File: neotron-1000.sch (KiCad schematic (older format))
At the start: 0 parts

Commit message: Initial peripheral layout and Cadding
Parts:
- added J?: Micro_SD_Card_Det, symbol Connector:Micro_SD_Card_Det
- added U?: STM32H743ZITx, Package_QFP:LQFP-144_20x20mm_P0.5mm, symbol MCU_ST_STM32H7:STM32H743ZITx
- added U?: AS4C4M16SA, TSOPII-54, symbol Memory_RAM:AS4C4M16SA
- added U?: TUSB2036, Package_QFP:LQFP-32_7x7mm_P0.8mm, symbol Interface_USB:TUSB2036
- added U?: TPS2042D, Package_SO:SOIC-8_3.9x4.9mm_P1.27mm, symbol Power_Management:TPS2042D
- added U?: ENC28J60x-SO, Package_SO:SOIC-28W_7.5x17.9mm_P1.27mm, symbol Interface_Ethernet:ENC28J60x-SO
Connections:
- new net: U?.10 (~OVRCUR1), U?.8 (~OC1)
- new net: U?.13 (~PWRON2), U?.4 (~EN2)
- new net: U?.14 (~OVRCUR2), U?.5 (~OC2)
- new net: U?.3 (~EN1), U?.9 (~PWRON1)
- new net ETH_SPI_MISO: U?.28 (PC2_C), U?.6 (SO)
- new net ETH_SPI_MOSI: U?.27 (PC1), U?.7 (SI)
- new net ETH_SPI_SCK: U?.101 (PA9), U?.8 (SCK)
- new net FMC_A0: U?.10 (PF0)
- new net FMC_A1: U?.11 (PF1)
- new net FMC_A10: U?.56 (PG0)
- new net FMC_A2: U?.12 (PF2)
- new net FMC_A3: U?.13 (PF3)
- new net FMC_A4: U?.14 (PF4)
- new net FMC_A5: U?.15 (PF5)
- new net FMC_A6: U?.50 (PF12)
- new net FMC_A7: U?.53 (PF13)
- new net FMC_A8: U?.54 (PF14)
- new net FMC_A9: U?.55 (PF15)
- new net FMC_BA0: U?.89 (PG4)
- new net FMC_CKE0: U?.29 (PC3_C)
- new net FMC_CLK: U?.93 (PG8)
- new net FMC_D0: U?.85 (PD14)
- new net FMC_D1: U?.86 (PD15)
- new net FMC_D2: U?.114 (PD0)
- new net FMC_D3: U?.115 (PD1)
- new net FMC_D4: U?.58 (PE7)
- new net FMC_D5: U?.59 (PE8)
- new net FMC_D6: U?.60 (PE9)
- new net FMC_D7: U?.63 (PE10)
- new net GND: J?.6 (VSS), U?.1 (GND), U?.107 (VSS), U?.11 (VSSRX), U?.120 (VSS), U?.130 (VSS), U?.16 (VSS), U?.18 (VSSTX), U?.2 (VSS), U?.21 (VSSPLL), U?.21 (~OCPROT~/~PWRSW~), U?.22 (NPINT0), U?.22 (VSSOSC), U?.23 (NPINT1), U?.28 (GND), U?.31 (MODE), U?.31 (VSSA), U?.38 (VSS), U?.51 (VSS), U?.61 (VSS), U?.7 (GND), U?.83 (VSS), U?.9 (~CS), U?.94 (VSS)
- new net GPU_INT: U?.118 (PD4)
- new net GPU_SPI_CLK: U?.126 (PG11)
- new net GPU_SPI_MIS0: U?.124 (PG9)
- new net GPU_SPI_MOSI: U?.123 (PD7)
- new net HEADER_00: U?.34 (PA0)
- new net HEADER_01: U?.100 (PA8)
- new net HEADER_02: U?.135 (PB5)
- new net HEADER_03: U?.73 (PB12)
- new net HEADER_04: U?.74 (PB13)
- new net HEADER_05: U?.7 (PC13)
- new net HEADER_06: U?.8 (PC14)
- new net HEADER_07: U?.9 (PC15)
- new net HEADER_08: U?.80 (PD11)
- new net HEADER_09: U?.141 (PE0)
- new net HEADER_10: U?.142 (PE1)
- new net HEADER_11: U?.2 (PE3)
- new net HEADER_12: U?.57 (PG1)
- new net HEADER_13: U?.87 (PG2)
- new net HEADER_14: U?.88 (PG3)
- new net HEADER_15: U?.90 (PG5)
- new net HEADER_16: U?.91 (PG6)
- new net HEADER_17: U?.127 (PG12)
- new net HEADER_18: U?.129 (PG14)
- new net HEADER_SPI_MISO: U?.66 (PE13)
- new net HEADER_SPI_MOSI: U?.67 (PE14)
- new net HEADER_SPI_SCK: U?.1 (PE2)
- new net HEADER_UART_RX: U?.78 (PD9)
- new net HEADER_UART_TX: U?.77 (PD8)
- new net I2C_HEADER_SCL: U?.81 (PD12)
- new net I2C_HEADER_SDA: U?.82 (PD13)
- new net I2C_INT_SCL: U?.136 (PB6)
- new net I2C_INT_SDA: U?.137 (PB7)
- new net I2S_SCK: U?.133 (PB3)
- new net I2S_SDI: U?.134 (PB4)
- new net I2S_SDO: U?.48 (PB2)
- new net I2S_WS: U?.110 (PA15)
- new net LTDC_B0: U?.3 (PE4)
- new net LTDC_B1: U?.102 (PA10)
- new net LTDC_B2: U?.125 (PG10)
- new net LTDC_B3: U?.79 (PD10)
- new net LTDC_B4: U?.65 (PE12)
- new net LTDC_B5: U?.37 (PA3)
- new net LTDC_B6: U?.139 (PB8)
- new net LTDC_B7: U?.140 (PB9)
- new net LTDC_CLK: U?.92 (PG7)
- new net LTDC_DE: U?.22 (PF10)
- new net LTDC_G0: U?.4 (PE5)
- new net LTDC_G1: U?.5 (PE6)
- new net LTDC_G2: U?.42 (PA6)
- new net LTDC_G3: U?.64 (PE11)
- new net LTDC_G4: U?.69 (PB10)
- new net LTDC_G5: U?.70 (PB11)
- new net LTDC_G6: U?.97 (PC7)
- new net LTDC_G7: U?.117 (PD3)
- new net LTDC_HSYNC: U?.96 (PC6)
- new net LTDC_R0: U?.128 (PG13)
- new net LTDC_R1: U?.36 (PA2)
- new net LTDC_R2: U?.35 (PA1)
- new net LTDC_R3: U?.46 (PB0)
- new net LTDC_R4: U?.41 (PA5)
- new net LTDC_R5: U?.26 (PC0)
- new net LTDC_R6: U?.47 (PB1)
- new net LTDC_R7: U?.68 (PE15)
- new net LTDC_VSYNC: U?.40 (PA4)
- new net PS2_KBD_CLK: U?.19 (PF7)
- new net PS2_KBD_DAT: U?.18 (PF6)
- new net PS2_MSE_CLK: U?.21 (PF9)
- new net PS2_MSE_DAT: U?.20 (PF8)
- new net SDMMC_CK: J?.5 (CLK), U?.113 (PC12)
- new net SDMMC_CMD: J?.3 (CMD), U?.116 (PD2)
- new net SDMMC_D0: J?.7 (DAT0), U?.98 (PC8)
- new net SDMMC_D1: J?.8 (DAT1), U?.99 (PC9)
- new net SDMMC_D2: J?.1 (DAT2), U?.111 (PC10)
- new net SDMMC_D3: J?.2 (DAT3/CD), U?.112 (PC11)
- new net SWCLK: U?.109 (PA14)
- new net SWDIO: U?.105 (PA13)
- new net UART_RX: U?.122 (PD6)
- new net UART_TX: U?.119 (PD5)
- new net USB1_PWR: U?.7 (OUT1)
- new net USB2_PWR: U?.6 (OUT2)
- new net USB_C_DM: U?.103 (PA11)
- new net USB_C_DP: U?.104 (PA12)
- new net USB_HOST_DM: U?.75 (PB14)
- new net USB_HOST_DP: U?.76 (PB15)
- new net VBUS: U?.2 (IN1)
- new net VCC: J?.4 (VDD), U?.108 (VDD), U?.121 (VDD), U?.131 (VDD), U?.144 (VDD), U?.15 (VDDTX), U?.17 (VDD), U?.19 (VDDRX), U?.20 (VDDPLL), U?.24 (~NP3), U?.25 (VCC), U?.25 (VDDOSC), U?.26 (~EXTMEM), U?.28 (VDD), U?.3 (VCC), U?.30 (VDD), U?.33 (VDDA), U?.39 (VDD), U?.52 (VDD), U?.6 (EEDATA/~GANGED), U?.6 (VBAT), U?.62 (VDD), U?.72 (VDD), U?.8 (~BUSPWR), U?.84 (VDD), U?.95 (VDD33_USB)
- new net ~ETH_INT: U?.4 (~INT), U?.45 (PC5)
- new net ~FMC_CAS: U?.132 (PG15)
- new net ~FMC_E0: U?.44 (PC4)
- new net ~FMC_RAS: U?.49 (PF11)
- new net ~FMC_WE: U?.43 (PA7)
- new net ~RESET: U?.10 (~RESET), U?.25 (NRST), U?.4 (~RESET)
- no-connect marks 0 -> 10

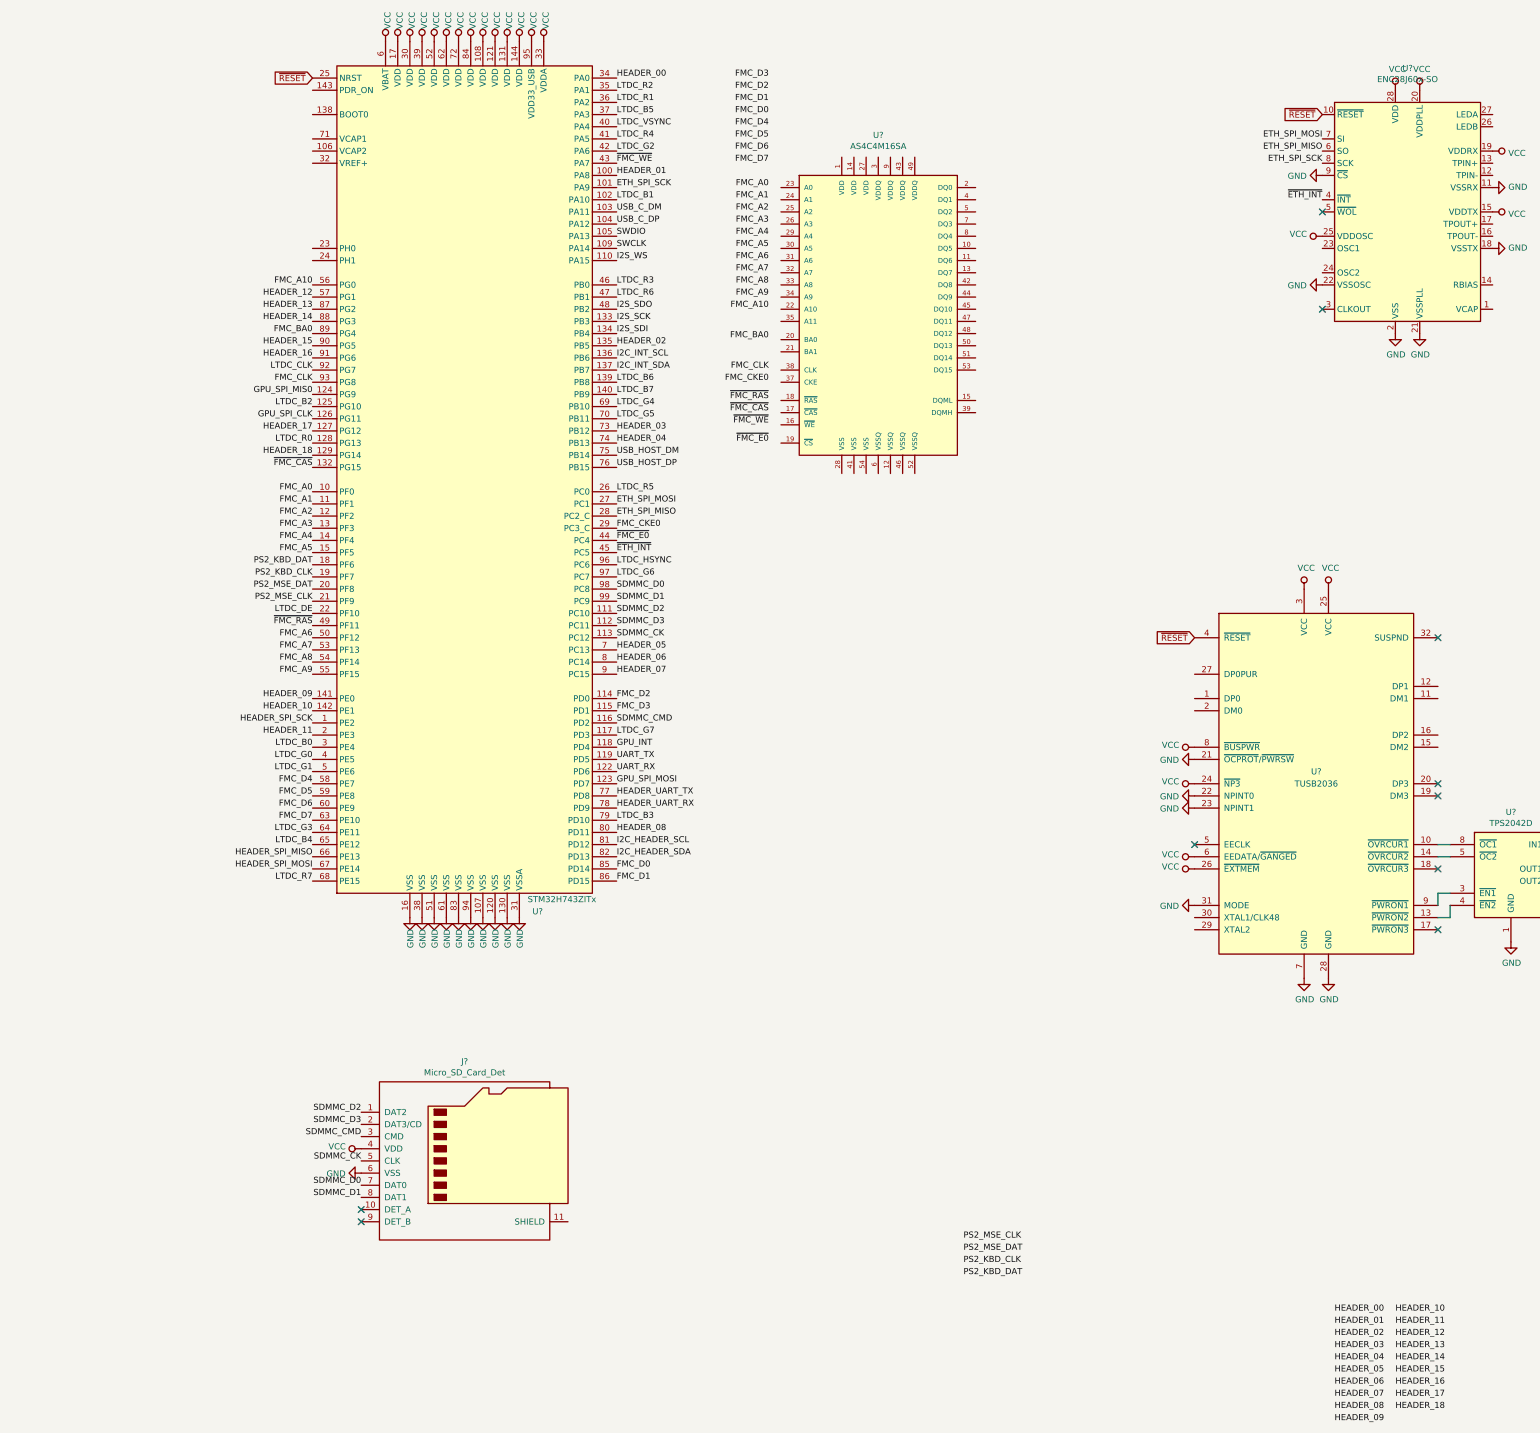
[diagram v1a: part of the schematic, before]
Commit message: added Pi Port
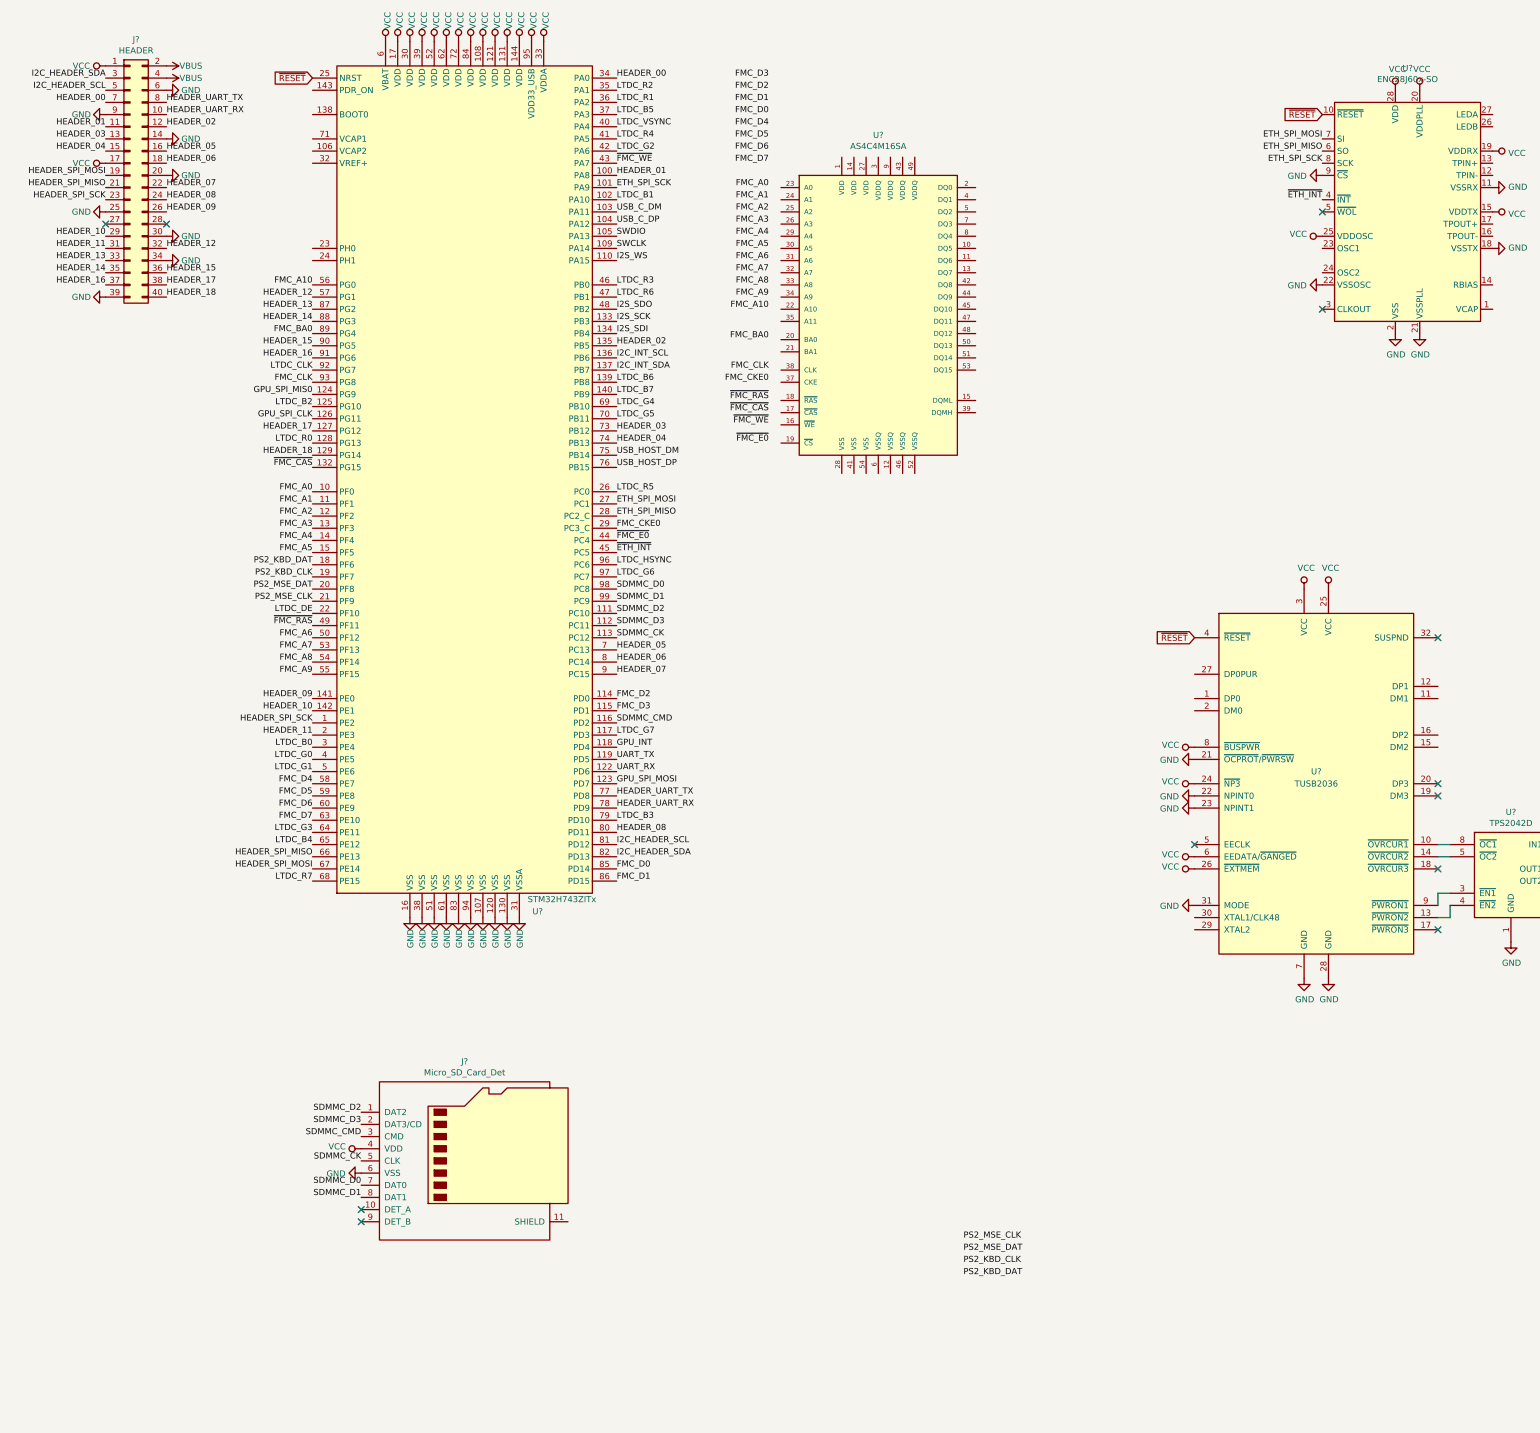
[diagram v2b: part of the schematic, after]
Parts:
- added J?: HEADER, symbol Connector_Generic:Conn_02x20_Odd_Even
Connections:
- net GND: now also J?.14 (Pin_14), J?.20 (Pin_20), J?.25 (Pin_25), J?.30 (Pin_30), J?.34 (Pin_34), J?.39 (Pin_39), J?.6 (Pin_6), J?.9 (Pin_9)
- net HEADER_00: now also J?.7 (Pin_7)
- net HEADER_01: now also J?.11 (Pin_11)
- net HEADER_02: now also J?.12 (Pin_12)
- net HEADER_03: now also J?.13 (Pin_13)
- net HEADER_04: now also J?.15 (Pin_15)
- net HEADER_05: now also J?.16 (Pin_16)
- net HEADER_06: now also J?.18 (Pin_18)
- net HEADER_07: now also J?.22 (Pin_22)
- net HEADER_08: now also J?.24 (Pin_24)
- net HEADER_09: now also J?.26 (Pin_26)
- net HEADER_10: now also J?.29 (Pin_29)
- net HEADER_11: now also J?.31 (Pin_31)
- net HEADER_12: now also J?.32 (Pin_32)
- net HEADER_13: now also J?.33 (Pin_33)
- net HEADER_14: now also J?.35 (Pin_35)
- net HEADER_15: now also J?.36 (Pin_36)
- net HEADER_16: now also J?.37 (Pin_37)
- net HEADER_17: now also J?.38 (Pin_38)
- net HEADER_18: now also J?.40 (Pin_40)
- net HEADER_SPI_MISO: now also J?.21 (Pin_21)
- net HEADER_SPI_MOSI: now also J?.19 (Pin_19)
- net HEADER_SPI_SCK: now also J?.23 (Pin_23)
- net HEADER_UART_RX: now also J?.10 (Pin_10)
- net HEADER_UART_TX: now also J?.8 (Pin_8)
- net I2C_HEADER_SCL: now also J?.5 (Pin_5)
- net I2C_HEADER_SDA: now also J?.3 (Pin_3)
- net VBUS: now also J?.2 (Pin_2), J?.4 (Pin_4)
- net VCC: now also J?.1 (Pin_1), J?.17 (Pin_17)
- no-connect marks 10 -> 12
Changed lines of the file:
@@
 Text Label 5850 7200 0    50   ~ 0
 GPU_INT
-Text Label 11750 11950 0    50   ~ 0
+Text Label 1650 2100 2    50   ~ 0
 HEADER_01
-Text Label 11750 12050 0    50   ~ 0
+Text Label 2150 2100 0    50   ~ 0
 HEADER_02
-Text Label 11750 12150 0    50   ~ 0
+Text Label 1650 2200 2    50   ~ 0
 HEADER_03
-Text Label 11750 12250 0    50   ~ 0
+Text Label 1650 2300 2    50   ~ 0
 HEADER_04
-Text Label 11750 12350 0    50   ~ 0
+Text Label 2150 2300 0    50   ~ 0
 HEADER_05
-Text Label 11750 12450 0    50   ~ 0
+Text Label 2150 2400 0    50   ~ 0
 HEADER_06
-Text Label 11750 12550 0    50   ~ 0
+Text Label 2150 2600 0    50   ~ 0
 HEADER_07
-Text Label 11750 11850 0    50   ~ 0
+Text Label 1650 1900 2    50   ~ 0
 HEADER_00
-Text Label 11750 12650 0    50   ~ 0
+Text Label 2150 2700 0    50   ~ 0
 HEADER_08
-Text Label 11750 12750 0    50   ~ 0
+Text Label 2150 2800 0    50   ~ 0
 HEADER_09
-Text Label 12250 11850 0    50   ~ 0
+Text Label 1650 3000 2    50   ~ 0
 HEADER_10
-Text Label 12250 11950 0    50   ~ 0
+Text Label 1650 3100 2    50   ~ 0
 HEADER_11
-Text Label 12250 12050 0    50   ~ 0
+Text Label 2150 3100 0    50   ~ 0
 HEADER_12
-Text Label 12250 12150 0    50   ~ 0
+Text Label 1650 3200 2    50   ~ 0
 HEADER_13
-Text Label 12250 12250 0    50   ~ 0
+Text Label 1650 3300 2    50   ~ 0
 HEADER_14
-Text Label 12250 12350 0    50   ~ 0
+Text Label 2150 3300 0    50   ~ 0
 HEADER_15
-Text Label 12250 12450 0    50   ~ 0
+Text Label 1650 3400 2    50   ~ 0
 HEADER_16
-Text Label 12250 12550 0    50   ~ 0
+Text Label 2150 3400 0    50   ~ 0
 HEADER_17
-Text Label 12250 12650 0    50   ~ 0
+Text Label 2150 3500 0    50   ~ 0
 HEADER_18
 Text Label 5850 2500 0    50   ~ 0
@@
 	1    0    0    -1
 $EndComp
+$Comp
+L Connector_Generic:Conn_02x20_Odd_Even J?
+U 1 1 5DC24F38
+P 1850 2500
+F 0 "J?" H 1900 3617 50  0000 C CNN
+F 1 "HEADER" H 1900 3526 50  0000 C CNN
+F 2 "" H 1850 2500 50  0001 C CNN
+F 3 "~" H 1850 2500 50  0001 C CNN
+	1    1850 2500
+	1    0    0    -1
+$EndComp
+NoConn ~ 2150 2900
+NoConn ~ 1650 2900
+$Comp
+L power:GND #PWR?
+U 1 1 5DC4AF6B
+P 1650 3500
+F 0 "#PWR?" H 1650 3250 50  0001 C CNN
+F 1 "GND" V 1650 3300 50  0000 C CNN
+F 2 "" H 1650 3500 50  0001 C CNN
+F 3 "" H 1650 3500 50  0001 C CNN
+	1    1650 3500
+	0    1    1    0
+$EndComp
+$Comp
+L power:GND #PWR?
+U 1 1 5DC4B37B
+P 2150 3200
+F 0 "#PWR?" H 2150 2950 50  0001 C CNN
+F 1 "GND" V 2150 3000 50  0000 C CNN
+F 2 "" H 2150 3200 50  0001 C CNN
+F 3 "" H 2150 3200 50  0001 C CNN
+	1    2150 3200
+	0    -1   -1   0
+$EndComp
+$Comp
+L power:GND #PWR?
+U 1 1 5DC4B92F
+P 2150 3000
+F 0 "#PWR?" H 2150 2750 50  0001 C CNN
+F 1 "GND" V 2150 2800 50  0000 C CNN
+F 2 "" H 2150 3000 50  0001 C CNN
+F 3 "" H 2150 3000 50  0001 C CNN
+	1    2150 3000
+	0    -1   -1   0
+$EndComp
+$Comp
+L power:GND #PWR?
+U 1 1 5DC4BF75
+P 1650 2800
+F 0 "#PWR?" H 1650 2550 50  0001 C CNN
+F 1 "GND" V 1650 2600 50  0000 C CNN
+F 2 "" H 1650 2800 50  0001 C CNN
+F 3 "" H 1650 2800 50  0001 C CNN
+	1    1650 2800
+	0    1    1    0
+$EndComp
+$Comp
+L power:GND #PWR?
+U 1 1 5DC4C2C4
+P 1650 2000
+F 0 "#PWR?" H 1650 1750 50  0001 C CNN
+F 1 "GND" V 1650 1800 50  0000 C CNN
+F 2 "" H 1650 2000 50  0001 C CNN
+F 3 "" H 1650 2000 50  0001 C CNN
+	1    1650 2000
+	0    1    1    0
+$EndComp
+$Comp
+L power:GND #PWR?
+U 1 1 5DC4DA01
+P 2150 2500
+F 0 "#PWR?" H 2150 2250 50  0001 C CNN
+F 1 "GND" V 2150 2300 50  0000 C CNN
+F 2 "" H 2150 2500 50  0001 C CNN
+F 3 "" H 2150 2500 50  0001 C CNN
+	1    2150 2500
+	0    -1   -1   0
+$EndComp
+$Comp
+L power:GND #PWR?
+U 1 1 5DC4DDE5
+P 2150 2200
+F 0 "#PWR?" H 2150 1950 50  0001 C CNN
+F 1 "GND" V 2150 2000 50  0000 C CNN
+F 2 "" H 2150 2200 50  0001 C CNN
+F 3 "" H 2150 2200 50  0001 C CNN
+	1    2150 2200
+	0    -1   -1   0
+$EndComp
+$Comp
+L power:GND #PWR?
+U 1 1 5DC4E165
+P 2150 1800
+F 0 "#PWR?" H 2150 1550 50  0001 C CNN
+F 1 "GND" V 2150 1600 50  0000 C CNN
+F 2 "" H 2150 1800 50  0001 C CNN
+F 3 "" H 2150 1800 50  0001 C CNN
+	1    2150 1800
+	0    -1   -1   0
+$EndComp
+$Comp
+L power:VBUS #PWR?
+U 1 1 5DC4E9A0
+P 2150 1700
+F 0 "#PWR?" H 2150 1550 50  0001 C CNN
+F 1 "VBUS" V 2150 1900 50  0000 C CNN
+F 2 "" H 2150 1700 50  0001 C CNN
+F 3 "" H 2150 1700 50  0001 C CNN
+	1    2150 1700
+	0    1    1    0
+$EndComp
+$Comp
+L power:VBUS #PWR?
+U 1 1 5DC4F818
+P 2150 1600
+F 0 "#PWR?" H 2150 1450 50  0001 C CNN
+F 1 "VBUS" V 2150 1800 50  0000 C CNN
+F 2 "" H 2150 1600 50  0001 C CNN
+F 3 "" H 2150 1600 50  0001 C CNN
+	1    2150 1600
+	0    1    1    0
+$EndComp
+$Comp
+L power:VCC #PWR?
+U 1 1 5DC504C5
+P 1650 1600
+F 0 "#PWR?" H 1650 1450 50  0001 C CNN
+F 1 "VCC" V 1650 1800 50  0000 C CNN
+F 2 "" H 1650 1600 50  0001 C CNN
+F 3 "" H 1650 1600 50  0001 C CNN
+	1    1650 1600
+	0    -1   -1   0
+$EndComp
+$Comp
+L power:VCC #PWR?
+U 1 1 5DC520AB
+P 1650 2400
+F 0 "#PWR?" H 1650 2250 50  0001 C CNN
+F 1 "VCC" V 1650 2600 50  0000 C CNN
+F 2 "" H 1650 2400 50  0001 C CNN
+F 3 "" H 1650 2400 50  0001 C CNN
+	1    1650 2400
+	0    -1   -1   0
+$EndComp
+Text Label 2150 1900 0    50   ~ 0
+HEADER_UART_TX
+Text Label 2150 2000 0    50   ~ 0
+HEADER_UART_RX
+Text Label 1650 1800 2    50   ~ 0
+I2C_HEADER_SCL
+Text Label 1650 1700 2    50   ~ 0
+I2C_HEADER_SDA
+Text Label 1650 2700 2    50   ~ 0
+HEADER_SPI_SCK
+Text Label 1650 2600 2    50   ~ 0
+HEADER_SPI_MISO
+Text Label 1650 2500 2    50   ~ 0
+HEADER_SPI_MOSI
 $EndSCHEMATC

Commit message: Added passives for ethernet
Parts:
- added C? (x2): 10nF, symbol Device:C_Small
- added C?: 10u, symbol Device:CP_Small
- added FB?: Ferrite_Bead, symbol Device:Ferrite_Bead
- added J?: RJ45_Amphenol_RJMG1BD3B8K1ANR, Connector_RJ:RJ45_Amphenol_RJMG1BD3B8K1ANR, symbol Connector:RJ45_Amphenol_RJMG1BD3B8K1ANR
- added R? (x4): 50R, symbol Device:R
- added R? (x2): 1K, symbol Device:R
- added R?: 2K, symbol Device:R
- added R?: 1K5, symbol Device:R
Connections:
- net GND: now also C?.2, C?.2, C?.2, J?.R8 (GND), R?.2
- net USB_HOST_DM: now also U?.2 (DM0)
- net USB_HOST_DP: now also U?.1 (DP0), R?.1
- net VCC: now also U?.13 (TPIN+), FB?.1, J?.L1 (LEDY_A), J?.L4 (LEDG_A), J?.R1 (TD+), R?.1
- net at U?.27 (DP0PUR): now also R?.2
- net at U?.1 (VCAP): now also C?.1
- net at U?.12 (TPIN-): now also J?.R2 (TD-), R?.2
- net at U?.14 (RBIAS): now also R?.1
- net at U?.16 (TPOUT-): now also J?.R6 (RD-), R?.2
- net at U?.17 (TPOUT+): now also J?.R3 (RD+), R?.1
- net at U?.26 (LEDB): now also R?.1
- net at U?.27 (LEDA): now also R?.1
- new net: C?.1, FB?.2, J?.R4 (TCT), R?.1, R?.2
- new net: C?.1, R?.1, R?.2
- new net ETH_LED_A: J?.L3 (LEDG_K), R?.2
- new net ETH_LED_B: J?.L2 (LEDY_K), R?.2
- no-connect marks 12 -> 13
